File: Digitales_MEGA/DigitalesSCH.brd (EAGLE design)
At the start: 92.5 x 59.6 mm, 23 parts

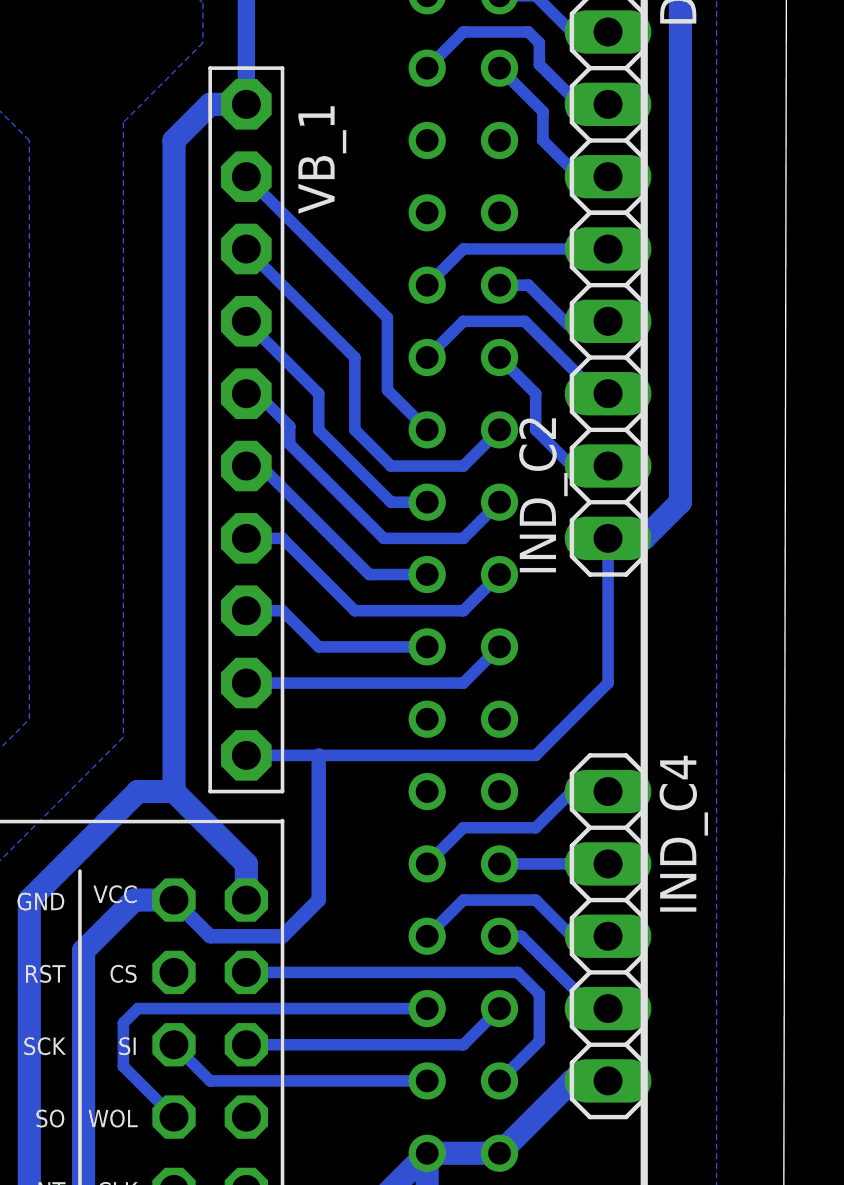
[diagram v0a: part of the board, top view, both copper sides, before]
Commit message: Programa p/el arduino mega. Modif nombres pinout
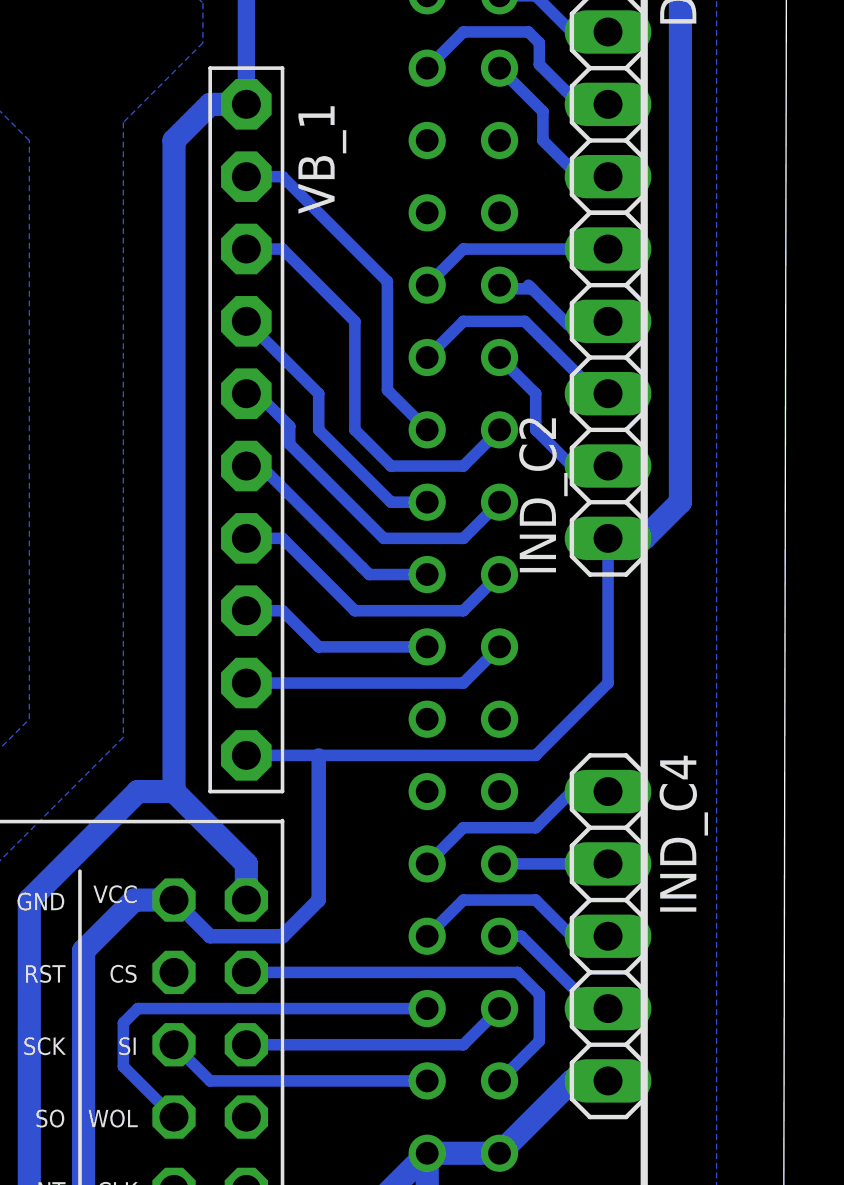
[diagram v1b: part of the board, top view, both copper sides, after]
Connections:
- removed net IND_4_C2: IND_C2.2, U$1.33
- removed net IND_4_C4: IND_C4.1, U$1.46
- removed net PUL_4_C2: U$1.34, VB_1.2
- removed net PUL_4_C4: U$1.38, VB_1.6
- new net IND_0_C2: IND_C2.5, U$1.30
- new net IND_0_C4: IND_C4.4, U$1.49
- new net PUL_0_C2: U$1.37, VB_1.5
- new net PUL_0_C4: U$1.41, VB_1.9
- net IND_1_C2: now also IND_C2.4, U$1.31; no longer IND_C2.5, U$1.30
- net IND_1_C4: now also IND_C4.3, U$1.48; no longer IND_C4.4, U$1.49
- net IND_2_C2: now also IND_C2.3, U$1.32; no longer IND_C2.4, U$1.31
- net IND_2_C4: now also IND_C4.2, U$1.47; no longer IND_C4.3, U$1.48
- net IND_3_C2: now also IND_C2.2, U$1.33; no longer IND_C2.3, U$1.32
- net IND_3_C4: now also IND_C4.1, U$1.46; no longer IND_C4.2, U$1.47
- net PUL_1_C2: now also U$1.36, VB_1.4; no longer U$1.37, VB_1.5
- net PUL_1_C4: now also U$1.40, VB_1.8; no longer U$1.41, VB_1.9
- net PUL_2_C2: now also U$1.35, VB_1.3; no longer U$1.36, VB_1.4
- net PUL_2_C4: now also U$1.39, VB_1.7; no longer U$1.40, VB_1.8
- net PUL_3_C2: now also U$1.34, VB_1.2; no longer U$1.35, VB_1.3
- net PUL_3_C4: now also U$1.38, VB_1.6; no longer U$1.39, VB_1.7
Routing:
- net PUL_4_C2: track 11.5 -> 0.00 mm
- net PUL_0_C2: track 0.00 -> 11.5 mm
- net PUL_0_C4: track 0.00 -> 9.42 mm
- net PUL_4_C4: track 7.93 -> 0.00 mm
- net IND_4_C4: track 7.40 -> 0.00 mm
- net IND_0_C2: track 0.00 -> 6.88 mm
- net IND_4_C2: track 6.13 -> 0.00 mm
- net PUL_2_C2: track 9.72 -> 14.8 mm
- net IND_0_C4: track 0.00 -> 4.86 mm
- net IND_2_C2: track 4.44 -> 8.08 mm
- net IND_3_C4: track 3.81 -> 7.40 mm
- net PUL_2_C4: track 6.88 -> 10.5 mm
- net IND_2_C4: track 7.40 -> 3.81 mm
- net PUL_1_C4: track 9.42 -> 6.88 mm
- net IND_1_C4: track 4.86 -> 7.40 mm
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
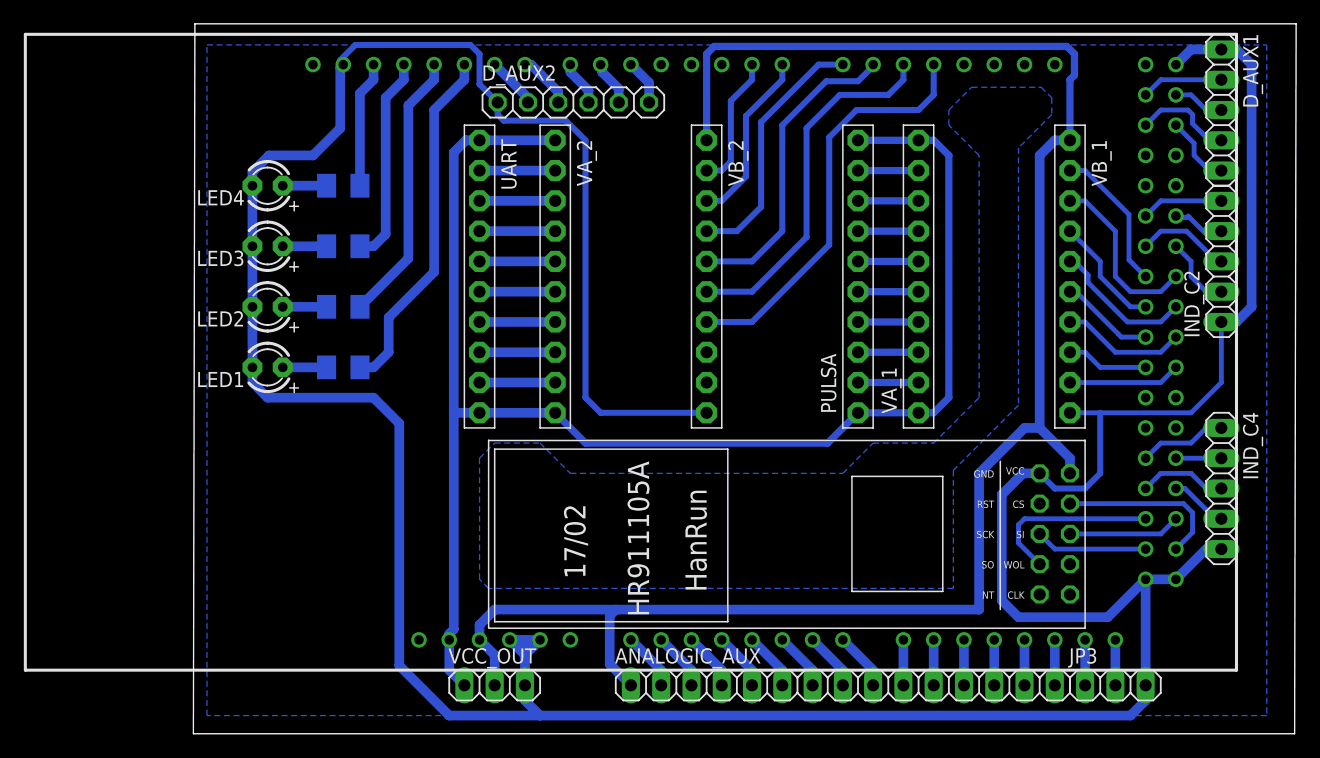
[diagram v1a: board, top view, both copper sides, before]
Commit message: Llave de encendico al esquematico y pcb
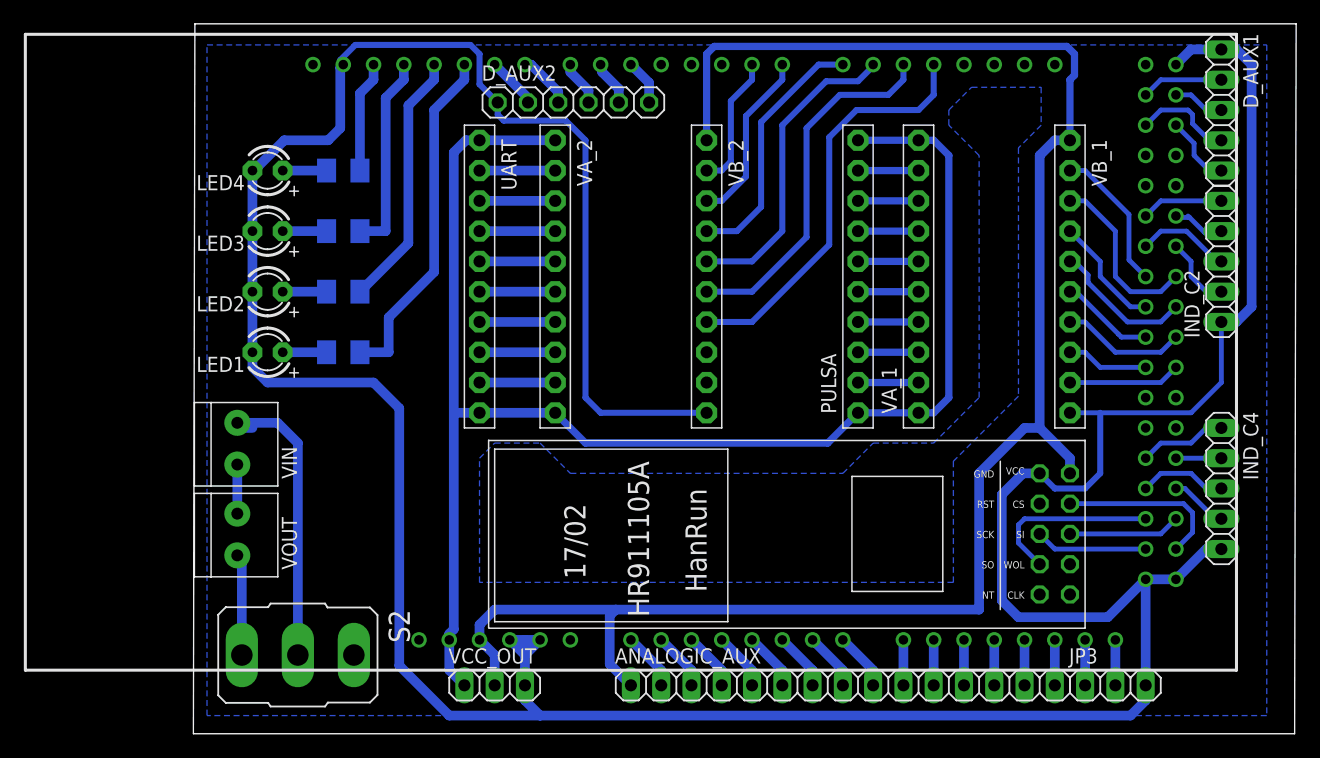
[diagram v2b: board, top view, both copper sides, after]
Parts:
- added S2: (no value), switch:M9040P
- added VIN, VOUT: 1X2-3.5MM, adafruit:1X2-3.5MM
- moved LED1 1.27 mm to (19.1, 33.0)
- moved LED2 1.27 mm to (19.1, 38.1)
- moved LED3 1.27 mm to (19.1, 43.2)
- moved R1 1.27 mm to (25.4, 33.0)
- moved R2 1.27 mm to (25.4, 38.1)
- moved R3 1.27 mm to (25.4, 43.2)
- moved LED4 1.27 mm to (19.1, 48.3)
- moved R4 1.27 mm to (25.4, 48.3)
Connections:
- new net N$14: S2.3, VOUT.1
- new net N$15: VIN.1, VOUT.2
- new net N$5: S2.2, VIN.2
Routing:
- net N$5: track 0.00 -> 25.0 mm
- net N$14: track 0.00 -> 8.52 mm
- net N$15: track 0.00 -> 4.12 mm
- net D11: track 22.9 -> 21.6 mm
- net D13: track 10.6 -> 9.36 mm
- net D12: track 17.4 -> 16.8 mm
- net D10: track 29.7 -> 29.2 mm

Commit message: Actaulización PCB y SCH
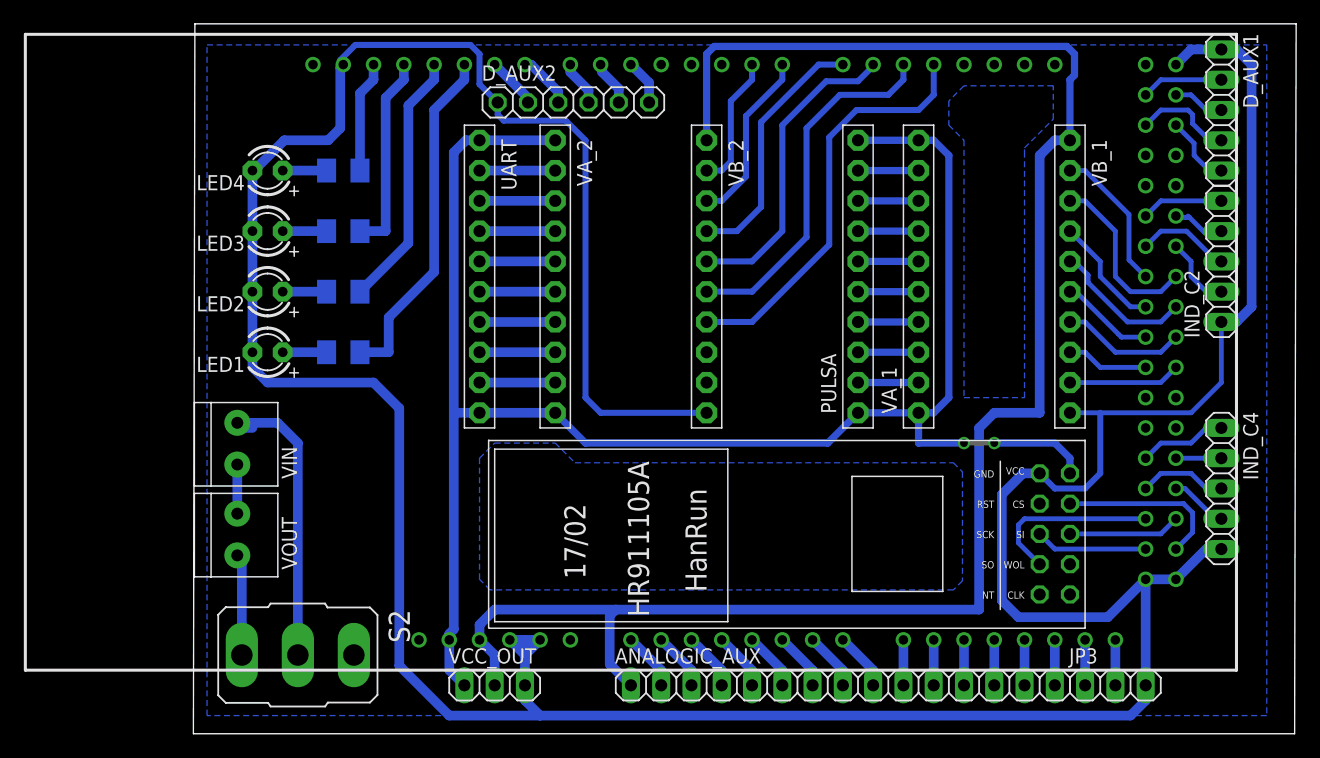
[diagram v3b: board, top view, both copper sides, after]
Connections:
- net 3V3: now also U$2.VCC
- net 5VDC: no longer U$2.VCC
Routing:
- net 3V3: track 126.9 -> 144.0 mm, vias 0 -> 2
- net 5VDC: track 150.2 -> 146.9 mm
- added copper zone on layer 16, net AA0
- added copper zone on layer 16, net AA1
- removed copper zone on layer 16, net A
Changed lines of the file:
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@@
 <grid distance="50" unitdist="mil" unit="mil" style="lines" multiple="1" display="no" altdistance="5" altunitdist="mil" altunit="mil"/>
 <layers>
-<layer number="1" name="Top" color="4" fill="1" visible="yes" active="yes"/>
+<layer number="1" name="Top" color="4" fill="1" visible="no" active="yes"/>
 <layer number="16" name="Bottom" color="1" fill="1" visible="yes" active="yes"/>
 <layer number="17" name="Pads" color="2" fill="1" visible="yes" active="yes"/>
@@
 <wire x1="76.2" y1="29.21" x2="76.2" y2="49.53" width="0.6096" layer="16"/>
 <wire x1="68.58" y1="50.8" x2="73.66" y2="50.8" width="0.6096" layer="16"/>
+<contactref element="U$2" pad="VCC"/>
+<wire x1="73.66" y1="27.94" x2="73.66" y2="25.4" width="0.6096" layer="16"/>
+<wire x1="73.66" y1="25.4" x2="77.47" y2="25.4" width="0.6096" layer="16"/>
+<wire x1="85.09" y1="25.4" x2="86.36" y2="24.13" width="0.6096" layer="16"/>
+<wire x1="86.36" y1="24.13" x2="86.36" y2="22.86" width="0.6096" layer="16"/>
+<wire x1="80.01" y1="25.4" x2="85.09" y2="25.4" width="0.6096" layer="16"/>
+<via x="77.47" y="25.4" extent="1-16" drill="0.65" diameter="0.55"/>
+<via x="80.01" y="25.4" extent="1-16" drill="0.65" diameter="0.55"/>
+<wire x1="77.47" y1="25.4" x2="80.01" y2="25.4" width="0.4064" layer="1"/>
 </signal>
 <signal name="5VDC">
@@
 <contactref element="VB_2" pad="1"/>
 <contactref element="VB_1" pad="1"/>
-<contactref element="U$2" pad="VCC"/>
 <wire x1="38.1" y1="7.62" x2="36.83" y2="8.89" width="0.8128" layer="16"/>
 <wire x1="38.1" y1="5.08" x2="38.1" y2="7.62" width="0.8128" layer="16"/>
 <wire x1="86.36" y1="50.8" x2="85.09" y2="50.8" width="0.8128" layer="16"/>
 <wire x1="85.09" y1="50.8" x2="83.82" y2="49.53" width="0.8128" layer="16"/>
-<wire x1="83.82" y1="49.53" x2="83.82" y2="26.67" width="0.8128" layer="16"/>
-<wire x1="83.82" y1="26.67" x2="86.36" y2="24.13" width="0.8128" layer="16"/>
-<wire x1="86.36" y1="24.13" x2="86.36" y2="22.86" width="0.8128" layer="16"/>
+<wire x1="83.82" y1="49.53" x2="83.82" y2="27.94" width="0.8128" layer="16"/>
 <wire x1="36.83" y1="8.89" x2="36.83" y2="10.16" width="0.8128" layer="16"/>
 <wire x1="36.83" y1="10.16" x2="38.1" y2="11.43" width="0.8128" layer="16"/>
 <wire x1="38.1" y1="11.43" x2="48.26" y2="11.43" width="0.8128" layer="16"/>
 <wire x1="48.26" y1="11.43" x2="78.74" y2="11.43" width="0.8128" layer="16"/>
-<wire x1="78.74" y1="11.43" x2="78.74" y2="22.86" width="0.8128" layer="16"/>
-<wire x1="78.74" y1="22.86" x2="82.55" y2="26.67" width="0.8128" layer="16"/>
-<wire x1="82.55" y1="26.67" x2="83.82" y2="26.67" width="0.8128" layer="16"/>
+<wire x1="78.74" y1="11.43" x2="78.74" y2="26.67" width="0.8128" layer="16"/>
+<wire x1="78.74" y1="26.67" x2="80.01" y2="27.94" width="0.8128" layer="16"/>
+<wire x1="80.01" y1="27.94" x2="83.82" y2="27.94" width="0.8128" layer="16"/>
 <wire x1="55.88" y1="50.8" x2="55.88" y2="58.039" width="0.6096" layer="16"/>
 <wire x1="55.88" y1="58.039" x2="56.515" y2="58.674" width="0.6096" layer="16"/>
@@
 <wire x1="51.054" y1="55.626" x2="51.054" y2="53.975" width="0.8128" layer="16"/>
 </signal>
-<signal name="A">
-<polygon width="0.8128" layer="16" spacing="1.778" isolate="0.8128">
-<vertex x="36.83" y="13.716"/>
-<vertex x="36.83" y="24.13"/>
-<vertex x="38.1" y="25.4"/>
-<vertex x="41.91" y="25.4"/>
-<vertex x="44.45" y="22.86"/>
-<vertex x="67.31" y="22.86"/>
-<vertex x="69.85" y="25.4"/>
-<vertex x="74.93" y="25.4"/>
-<vertex x="78.74" y="29.21"/>
-<vertex x="78.74" y="49.53"/>
-<vertex x="76.2" y="52.07"/>
-<vertex x="76.2" y="53.34"/>
-<vertex x="78.105" y="55.245"/>
-<vertex x="83.947" y="55.245"/>
-<vertex x="83.947" y="52.07"/>
-<vertex x="82.042" y="50.165"/>
-<vertex x="82.042" y="29.337"/>
-<vertex x="76.581" y="23.876"/>
-<vertex x="76.581" y="13.716"/>
-</polygon>
-</signal>
 <signal name="IND_0_C4">
 <contactref element="U$1" pad="49"/>
@@
 <wire x1="16.51" y1="23.6" x2="16.51" y2="19.48" width="0.8128" layer="16"/>
 </signal>
+<signal name="AA0">
+<polygon width="0.4064" layer="16">
+<vertex x="36.83" y="13.97"/>
+<vertex x="36.83" y="24.13"/>
+<vertex x="38.1" y="25.4"/>
+<vertex x="43.18" y="25.4"/>
+<vertex x="44.831" y="23.749"/>
+<vertex x="76.581" y="23.749"/>
+<vertex x="77.343" y="22.987"/>
+<vertex x="77.343" y="13.843"/>
+<vertex x="76.581" y="13.081"/>
+<vertex x="37.719" y="13.081"/>
+</polygon>
+</signal>
+<signal name="AA1">
+<polygon width="0.4064" layer="16">
+<vertex x="77.47" y="29.21"/>
+<vertex x="82.55" y="29.21"/>
+<vertex x="82.55" y="49.53"/>
+<vertex x="82.55" y="50.165"/>
+<vertex x="84.963" y="52.578"/>
+<vertex x="84.963" y="55.372"/>
+<vertex x="77.47" y="55.372"/>
+<vertex x="76.2" y="54.102"/>
+<vertex x="76.2" y="52.07"/>
+<vertex x="77.47" y="50.8"/>
+</polygon>
+</signal>
 </signals>
